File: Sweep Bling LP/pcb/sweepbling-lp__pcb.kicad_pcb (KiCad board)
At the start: 2 copper layers, 216.9 x 86.9 mm, 59 parts, among them SW1 SW_Push, SW10 SW_Push, SW10_r1 SW_Push, SW11 SW_Push, SW11_r1 SW_Push, SW12 SW_Push, SW12_r1 SW_Push, SW13 SW_Push, SW13_r1 SW_Push, SW14 SW_Push, SW14_r1 SW_Push, SW15 SW_Push, SW15_r1 SW_Push, SW16 SW_Push, SW16_r1 SW_Push, SW17 SW_Push, SW17_r1 SW_Push, SW1_r1 SW_Push, SW2 SW_Push, SW2_r1 SW_Push, SW3 SW_Push, SW3_r1 SW_Push, SW4 SW_Push, SW4_r1 SW_Push, SW5 SW_Push, SW5_r1 SW_Push, SW6 SW_Push, SW6_r1 SW_Push, SW7 SW_Push, SW7_r1 SW_Push, SW8 SW_Push, SW8_r1 SW_Push, SW9 SW_Push, SW9_r1 SW_Push, U1 ProMicro-kbd, U2 ProMicro-kbd

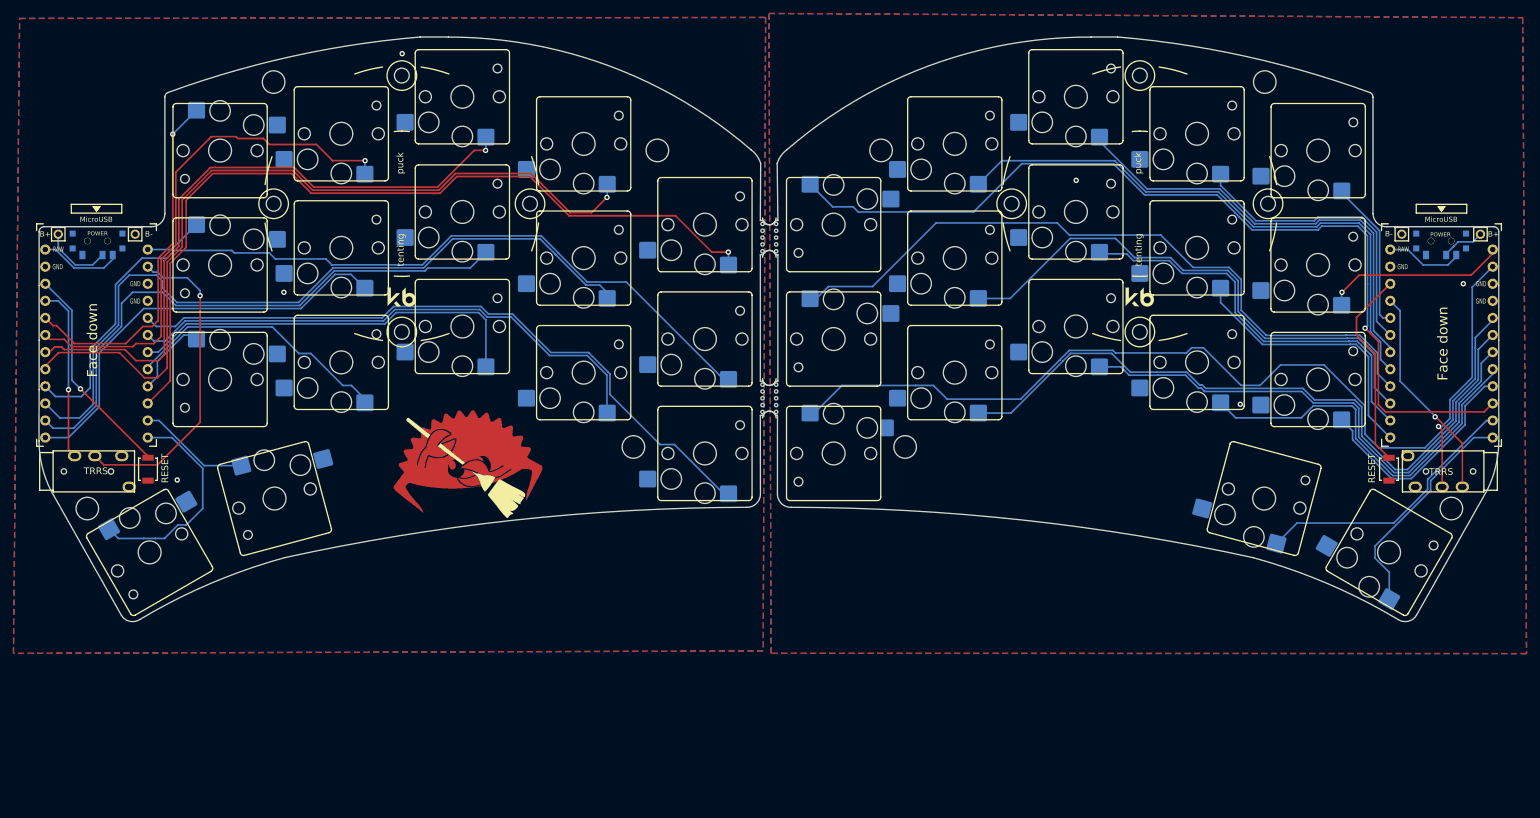
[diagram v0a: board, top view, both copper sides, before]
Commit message: edited Blink_LP
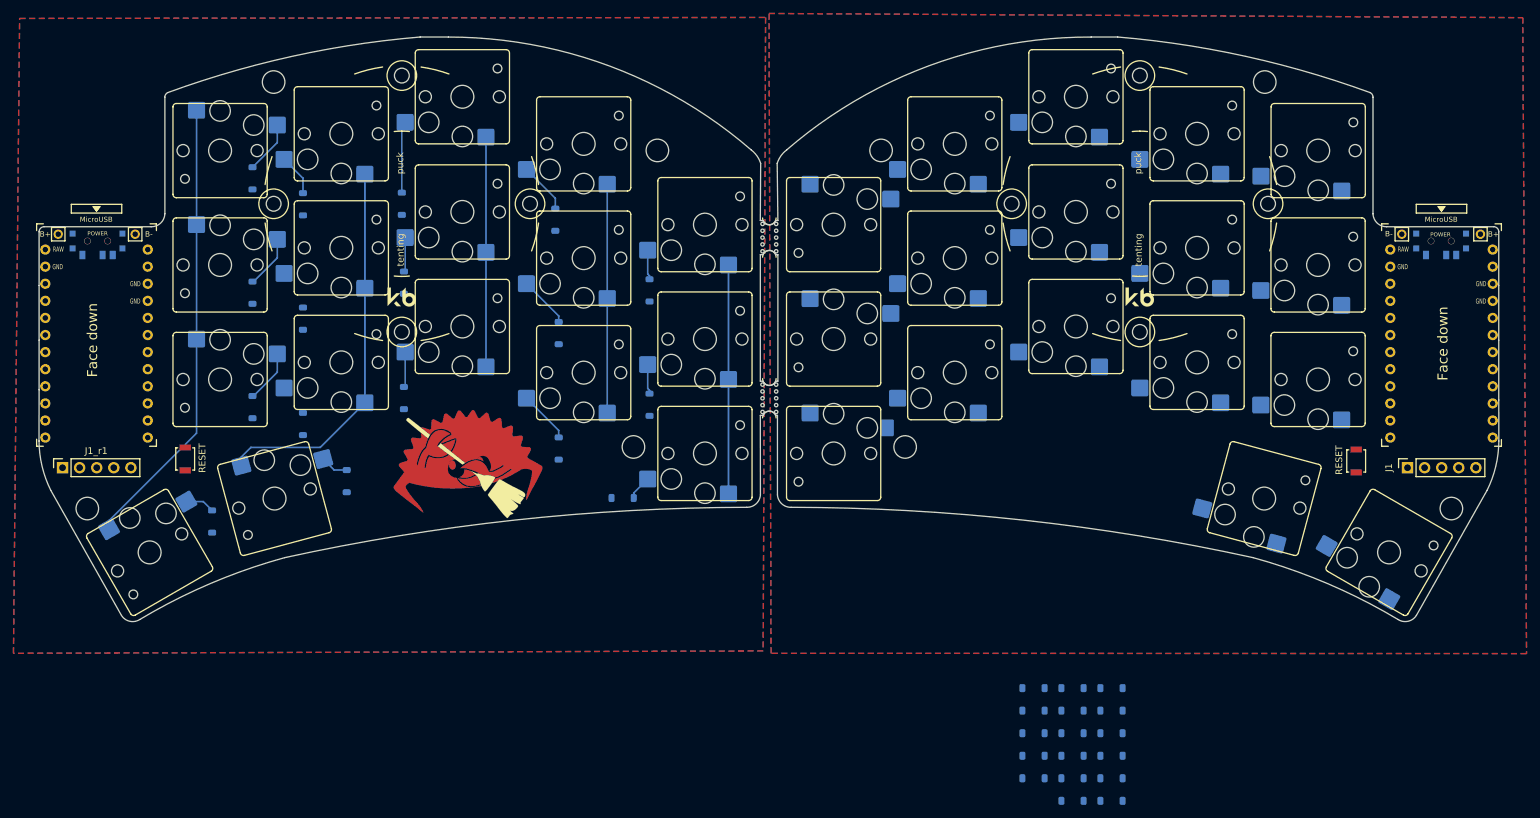
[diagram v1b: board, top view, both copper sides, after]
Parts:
- removed TRRS1, TRRS2: AudioJack4, * duckyb-collection:TRRS-PJ-320A
- added D1: 1N4148W, Diode_SMD:D_SOD-123, B.Cu at (53.5, 42.5)
- added D10: 1N4148W, Diode_SMD:D_SOD-123, B.Cu at (76.0, 58.0)
- added D11: 1N4148W, Diode_SMD:D_SOD-123, B.Cu at (76.0, 75.2)
- added D12: 1N4148W, Diode_SMD:D_SOD-123, B.Cu at (99.0, 82.7)
- added D13: 1N4148W, Diode_SMD:D_SOD-123, B.Cu at (99.0, 65.5)
- added D14: 1N4148W, Diode_SMD:D_SOD-123, B.Cu at (98.5, 48.6)
- added D15: 1N4148W, Diode_SMD:D_SOD-123, B.Cu at (112.5, 59.1)
- added D16: 1N4148W, Diode_SMD:D_SOD-123, B.Cu at (112.5, 76.2)
- added D17: 1N4148W, Diode_SMD:D_SOD-123, B.Cu at (108.5, 90.0)
- added D18: 1N4148W, Diode_SMD:D_SOD-123, B.Cu at (181.1, 118.2)
- added D19: 1N4148W, Diode_SMD:D_SOD-123, B.Cu at (181.1, 121.6)
- added D2: 1N4148W, Diode_SMD:D_SOD-123, B.Cu at (53.5, 59.5)
- added D20: 1N4148W, Diode_SMD:D_SOD-123, B.Cu at (181.1, 125.0)
- added D21: 1N4148W, Diode_SMD:D_SOD-123, B.Cu at (181.1, 128.3)
- added D22: 1N4148W, Diode_SMD:D_SOD-123, B.Cu at (181.1, 131.7)
- added D23: 1N4148W, Diode_SMD:D_SOD-123, B.Cu at (181.1, 135.0)
- added D24: 1N4148W, Diode_SMD:D_SOD-123, B.Cu at (175.3, 118.2)
- added D25: 1N4148W, Diode_SMD:D_SOD-123, B.Cu at (175.3, 121.6)
- added D26: 1N4148W, Diode_SMD:D_SOD-123, B.Cu at (175.3, 125.0)
- added D27: 1N4148W, Diode_SMD:D_SOD-123, B.Cu at (175.3, 128.3)
- added D28: 1N4148W, Diode_SMD:D_SOD-123, B.Cu at (175.3, 131.7)
- added D29: 1N4148W, Diode_SMD:D_SOD-123, B.Cu at (175.3, 135.0)
- added D3: 1N4148W, Diode_SMD:D_SOD-123, B.Cu at (53.5, 76.5)
- added D30: 1N4148W, Diode_SMD:D_SOD-123, B.Cu at (169.6, 118.2)
- added D31: 1N4148W, Diode_SMD:D_SOD-123, B.Cu at (169.6, 121.6)
- added D32: 1N4148W, Diode_SMD:D_SOD-123, B.Cu at (169.6, 125.0)
- added D33: 1N4148W, Diode_SMD:D_SOD-123, B.Cu at (169.6, 128.3)
- added D34: 1N4148W, Diode_SMD:D_SOD-123, B.Cu at (169.6, 131.7)
- added D4: 1N4148W, Diode_SMD:D_SOD-123, B.Cu at (47.5, 93.5)
- added D5: 1N4148W, Diode_SMD:D_SOD-123, B.Cu at (67.5, 87.5)
- added D6: 1N4148W, Diode_SMD:D_SOD-123, B.Cu at (61.0, 79.0)
- added D7: 1N4148W, Diode_SMD:D_SOD-123, B.Cu at (61.0, 63.4)
- added D8: 1N4148W, Diode_SMD:D_SOD-123, B.Cu at (61.0, 46.4)
- added D9: 1N4148W, Diode_SMD:D_SOD-123, B.Cu at (75.7, 46.3)
- added J1: Conn_01x05, Connector_PinSocket_2.54mm:PinSocket_1x05_P2.54mm_Vertical, F.Cu at (225.1, 85.5)
- added J1_r1: Conn_01x05, Connector_PinSocket_2.54mm:PinSocket_1x05_P2.54mm_Vertical, F.Cu at (25.3, 85.5)
- moved RSW2 5.73 mm to (43.5, 84.2)
- moved RSW1 5.03 mm to (217.5, 84.5)
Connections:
- SW1 pad 2: gnd -> Net-(D18-A)
- SW10 pad 1: Switch10 -> Switch5
- SW10 pad 2: gnd -> Net-(D27-A)
- SW10_r1 pad 1: Switch10_r -> Switch5_r
- SW10_r1 pad 2: gnd_r -> Net-(D2-A)
- SW11 pad 1: Switch11 -> Switch1
- SW11 pad 2: gnd -> Net-(D28-A)
- SW11_r1 pad 1: Switch11_r -> Switch1_r
- SW11_r1 pad 2: gnd_r -> Net-(D17-A)
- SW12 pad 1: Switch12 -> Switch2
- SW12 pad 2: gnd -> Net-(D29-A)
- SW12_r1 pad 1: Switch12_r -> Switch2_r
- SW12_r1 pad 2: gnd_r -> Net-(D12-A)
- SW13 pad 1: Switch13 -> Switch3
- SW13 pad 2: gnd -> Net-(D30-A)
- SW13_r1 pad 1: Switch13_r -> Switch3_r
- SW13_r1 pad 2: gnd_r -> Net-(D11-A)
- SW14 pad 1: Switch14 -> Switch4
- SW14 pad 2: gnd -> Net-(D31-A)
- SW14_r1 pad 1: Switch14_r -> Switch4_r
- SW14_r1 pad 2: gnd_r -> Net-(D6-A)
- SW15 pad 1: Switch15 -> Switch5
- SW15 pad 2: gnd -> Net-(D32-A)
- SW15_r1 pad 1: Switch15_r -> Switch5_r
- SW15_r1 pad 2: gnd_r -> Net-(D3-A)
- SW16 pad 1: Switch16 -> Switch4
- SW16 pad 2: gnd -> Net-(D33-A)
- SW16_r1 pad 1: Switch16_r -> Switch4_r
- SW16_r1 pad 2: gnd_r -> Net-(D5-A)
- SW17 pad 1: Switch17 -> Switch5
- SW17 pad 2: gnd -> Net-(D34-A)
- SW17_r1 pad 1: Switch17_r -> Switch5_r
- SW17_r1 pad 2: gnd_r -> Net-(D4-A)
- SW1_r1 pad 2: gnd_r -> Net-(D15-A)
- SW2 pad 2: gnd -> Net-(D19-A)
- SW2_r1 pad 2: gnd_r -> Net-(D14-A)
- SW3 pad 2: gnd -> Net-(D20-A)
- SW3_r1 pad 2: gnd_r -> Net-(D9-A)
- SW4 pad 2: gnd -> Net-(D21-A)
- SW4_r1 pad 2: gnd_r -> Net-(D8-A)
- SW5 pad 2: gnd -> Net-(D22-A)
- SW5_r1 pad 2: gnd_r -> Net-(D1-A)
- SW6 pad 1: Switch6 -> Switch1
- SW6 pad 2: gnd -> Net-(D23-A)
- SW6_r1 pad 1: Switch6_r -> Switch1_r
- SW6_r1 pad 2: gnd_r -> Net-(D16-A)
- SW7 pad 1: Switch7 -> Switch2
- SW7 pad 2: gnd -> Net-(D24-A)
- SW7_r1 pad 1: Switch7_r -> Switch2_r
- SW7_r1 pad 2: gnd_r -> Net-(D13-A)
- SW8 pad 1: Switch8 -> Switch3
- SW8 pad 2: gnd -> Net-(D25-A)
- SW8_r1 pad 1: Switch8_r -> Switch3_r
- SW8_r1 pad 2: gnd_r -> Net-(D10-A)
- SW9 pad 1: Switch9 -> Switch4
- SW9 pad 2: gnd -> Net-(D26-A)
- SW9_r1 pad 1: Switch9_r -> Switch4_r
- SW9_r1 pad 2: gnd_r -> Net-(D7-A)
- U1 pad 1: Switch10 -> CS
- U1 pad 13: Switch9 -> unconnected-(U1-B6-Pad13)
- U1 pad 14: Switch8 -> unconnected-(U1-B2-Pad14)
- U1 pad 15: Switch7 -> unconnected-(U1-B3-Pad15)
- U1 pad 16: Switch6 -> unconnected-(U1-B1-Pad16)
- U1 pad 2: Switch18 -> unconnected-(U1-RX-Pad2)
- U1 pad 5: Switch11 -> MOSI
- U1 pad 6: Switch12 -> SCK
- U2 pad 1: Switch10_r -> CS_r
- U2 pad 13: Switch9_r -> unconnected-(U2-B6-Pad13)
- U2 pad 14: Switch8_r -> unconnected-(U2-B2-Pad14)
- U2 pad 15: Switch7_r -> unconnected-(U2-B3-Pad15)
- U2 pad 16: Switch6_r -> unconnected-(U2-B1-Pad16)
- U2 pad 2: Switch18_r -> unconnected-(U2-RX-Pad2)
- U2 pad 5: Switch11_r -> MOSI_r
- U2 pad 6: Switch12_r -> SCK_r
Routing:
- net Switch1: track 136.4 -> 0.00 mm, vias 1 -> 0
- net Switch11: track 132.0 -> 0.00 mm
- net Switch6_r: track 129.4 -> 0.00 mm
- net Switch7_r: track 111.7 -> 0.00 mm
- net Switch6: track 105.4 -> 0.00 mm
- net Switch12: track 102.4 -> 0.00 mm
- net Switch11_r: track 101.4 -> 0.00 mm
- net Switch1_r: track 123.6 -> 34.0 mm, vias 1 -> 0
- net Switch2: track 86.0 -> 0.00 mm
- net Switch2_r: track 119.9 -> 34.0 mm, vias 1 -> 0
- net Switch8_r: track 85.1 -> 0.00 mm
- net Switch7: track 80.7 -> 0.00 mm
- net Switch12_r: track 80.2 -> 0.00 mm
- net Switch13: track 78.1 -> 0.00 mm
- net Switch3: track 66.1 -> 0.00 mm
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
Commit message: traces addition
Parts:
- moved D20 84.7 mm to (170.0, 41.0), turned to 90 degrees
- moved D22 83.1 mm to (203.0, 51.5), turned to 90 degrees
- moved D21 82.4 mm to (185.2, 46.0), turned to 90 degrees
- moved D19 79.1 mm to (152.5, 47.9), turned to 90 degrees
- moved D18 74.9 mm to (148.5, 50.9), turned to 90 degrees
- moved D23 73.6 mm to (148.5, 69.0), turned to 90 degrees
- moved D27 69.1 mm to (203.0, 65.0), turned to 90 degrees
- moved D25 64.1 mm to (167.5, 58.0), turned to 90 degrees
- moved D26 63.7 mm to (189.5, 62.9), turned to 90 degrees
- moved D34 59.6 mm to (214.0, 92.0), turned to -90 degrees
- moved D24 58.6 mm to (152.0, 64.5), turned to 90 degrees
- moved D29 56.4 mm to (157.5, 81.5)
- moved D32 54.4 mm to (203.5, 82.5), turned to 90 degrees
- moved D28 51.8 mm to (147.5, 88.0)
- moved D31 44.4 mm to (190.5, 82.5), turned to 90 degrees
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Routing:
- net Switch1: track 0.00 -> 154.1 mm, vias 0 -> 3
- net Switch14_r: track 0.00 -> 147.9 mm, vias 0 -> 1
- net Switch2_r: track 34.0 -> 142.1 mm, vias 0 -> 1
- net Switch15: track 0.00 -> 108.0 mm, vias 0 -> 7
- net Switch2: track 0.00 -> 107.8 mm, vias 0 -> 1
- net Switch15_r: track 0.00 -> 106.3 mm, vias 0 -> 3
- net Switch14: track 0.00 -> 105.1 mm, vias 0 -> 7
- net Switch16: track 0.00 -> 99.7 mm, vias 0 -> 3
- net Switch4: track 0.00 -> 95.5 mm, vias 0 -> 1
- net Switch1_r: track 34.0 -> 129.3 mm, vias 0 -> 1
- net Switch3_r: track 34.1 -> 121.9 mm, vias 0 -> 1
- net Switch5: track 0.00 -> 86.0 mm, vias 0 -> 1
- net Switch16_r: track 0.00 -> 77.4 mm, vias 0 -> 3
- net Switch17: track 0.00 -> 58.4 mm, vias 0 -> 3
- net Switch17_r: track 0.00 -> 43.4 mm, vias 0 -> 1
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
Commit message: traces
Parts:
- moved D9 6.32 mm to (79.0, 40.9)
- moved D22 5.06 mm to (207.3, 48.8)
- moved D33 4.82 mm to (195.6, 95.5), turned to 180 degrees
- moved D18 3.32 mm to (146.3, 53.3)
- moved D10 3.25 mm to (79.2, 57.9)
- moved D27 3.10 mm to (206.0, 65.8)
- moved D21 3.02 mm to (188.2, 46.2)
- moved D30 2.93 mm to (170.4, 75.4)
- moved D25 2.93 mm to (170.4, 58.0)
- moved D11 2.79 mm to (78.7, 75.7)
- moved D23 2.72 mm to (146.3, 70.6)
- moved D32 2.62 mm to (206.0, 83.3)
- moved D16 2.62 mm to (115.1, 76.7)
- moved D15 2.62 mm to (115.1, 59.7)
- moved D31 2.48 mm to (188.7, 80.8)
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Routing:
- net Switch3: track 34.1 -> 101.9 mm, vias 0 -> 5
- net Switch14_r: track 147.9 -> 110.5 mm, vias 1 -> 3
- net Switch5: track 86.0 -> 55.9 mm, vias 1 -> 2
- net reset: track 26.7 -> 0.00 mm, vias 1 -> 0
- net Switch4_r: track 98.6 -> 116.4 mm, vias 1 -> 7
- net Switch1_r: track 129.3 -> 145.9 mm
- net Switch5_r: track 104.7 -> 117.3 mm, vias 0 -> 1
- net Switch14: track 105.1 -> 115.8 mm, vias 7 -> 0
- net Switch17: track 58.4 -> 49.1 mm, vias 3 -> 0
- net Net-(D3-A): track 7.87 -> 0.00 mm
- net vcc_r: track 28.0 -> 34.8 mm, vias 1 -> 0
- net Switch2_r: track 142.1 -> 135.5 mm, vias 1 -> 5
- net Net-(D25-A): track 0.00 -> 6.34 mm
- net Net-(D7-A): track 0.00 -> 6.23 mm
- net Net-(D6-A): track 0.00 -> 5.70 mm
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
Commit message: DRC
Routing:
- net reset: track 0.00 -> 30.3 mm
- net Switch5: track 55.9 -> 85.6 mm, vias 2 -> 4
- net Net-(D3-A): track 0.00 -> 8.04 mm
- net BT+: track 6.46 -> 12.1 mm, vias 0 -> 1
- net gnd_r: vias 18 -> 26
- net gnd: vias 0 -> 22
